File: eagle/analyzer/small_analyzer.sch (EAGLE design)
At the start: 19 parts, among them IC1 MCP604ST, IC2 TPS77301

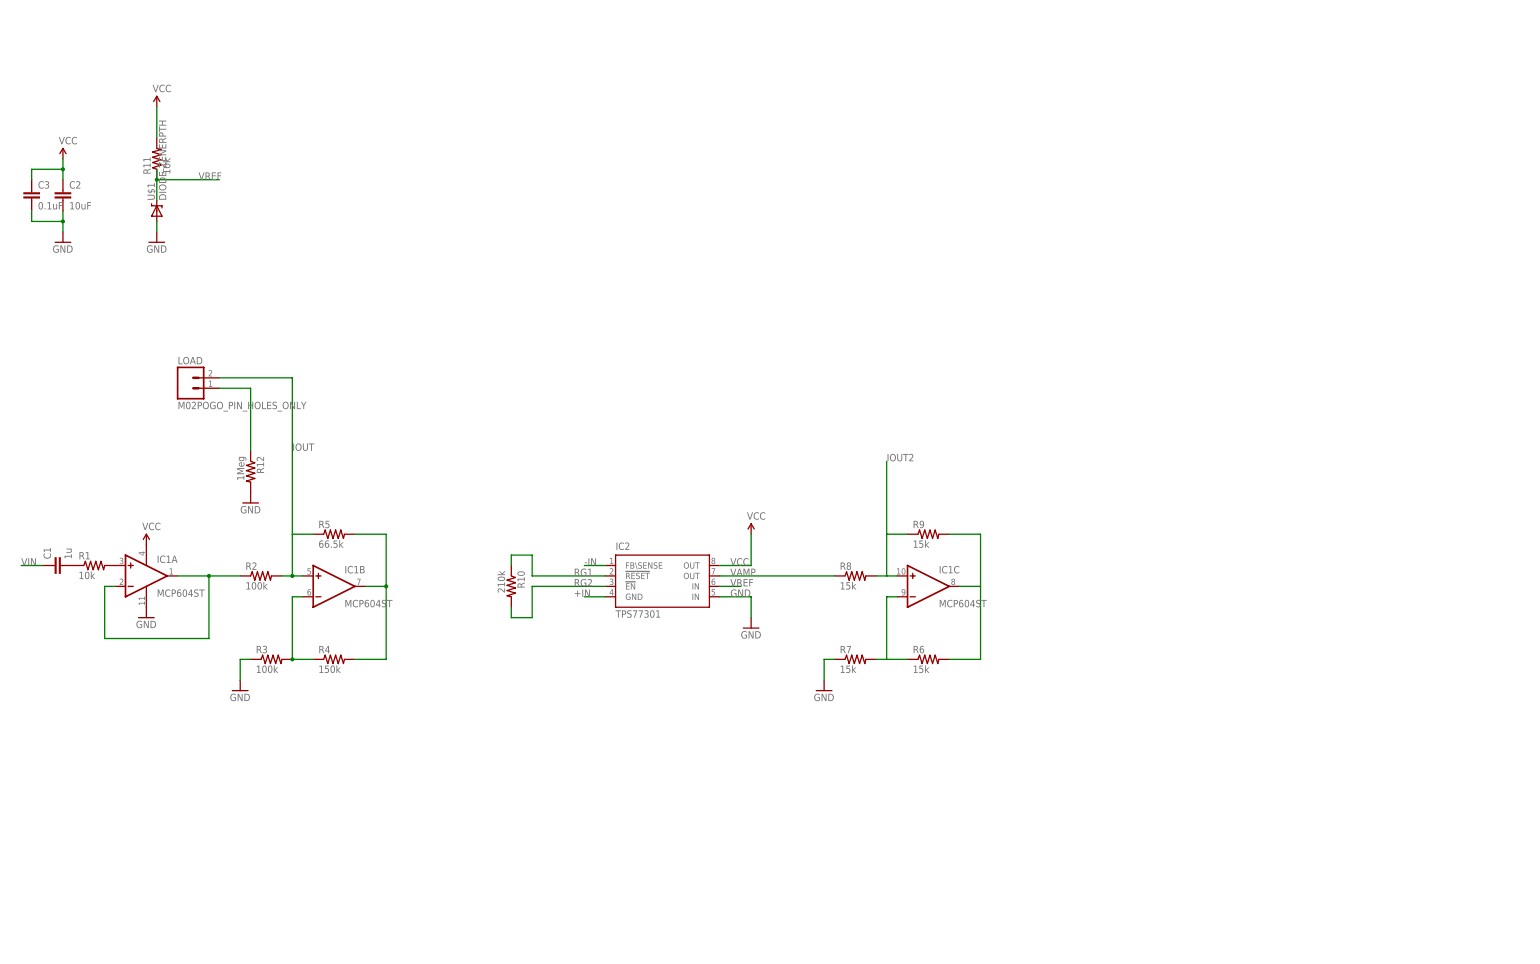
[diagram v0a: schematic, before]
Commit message: added analyzer ic with mcu
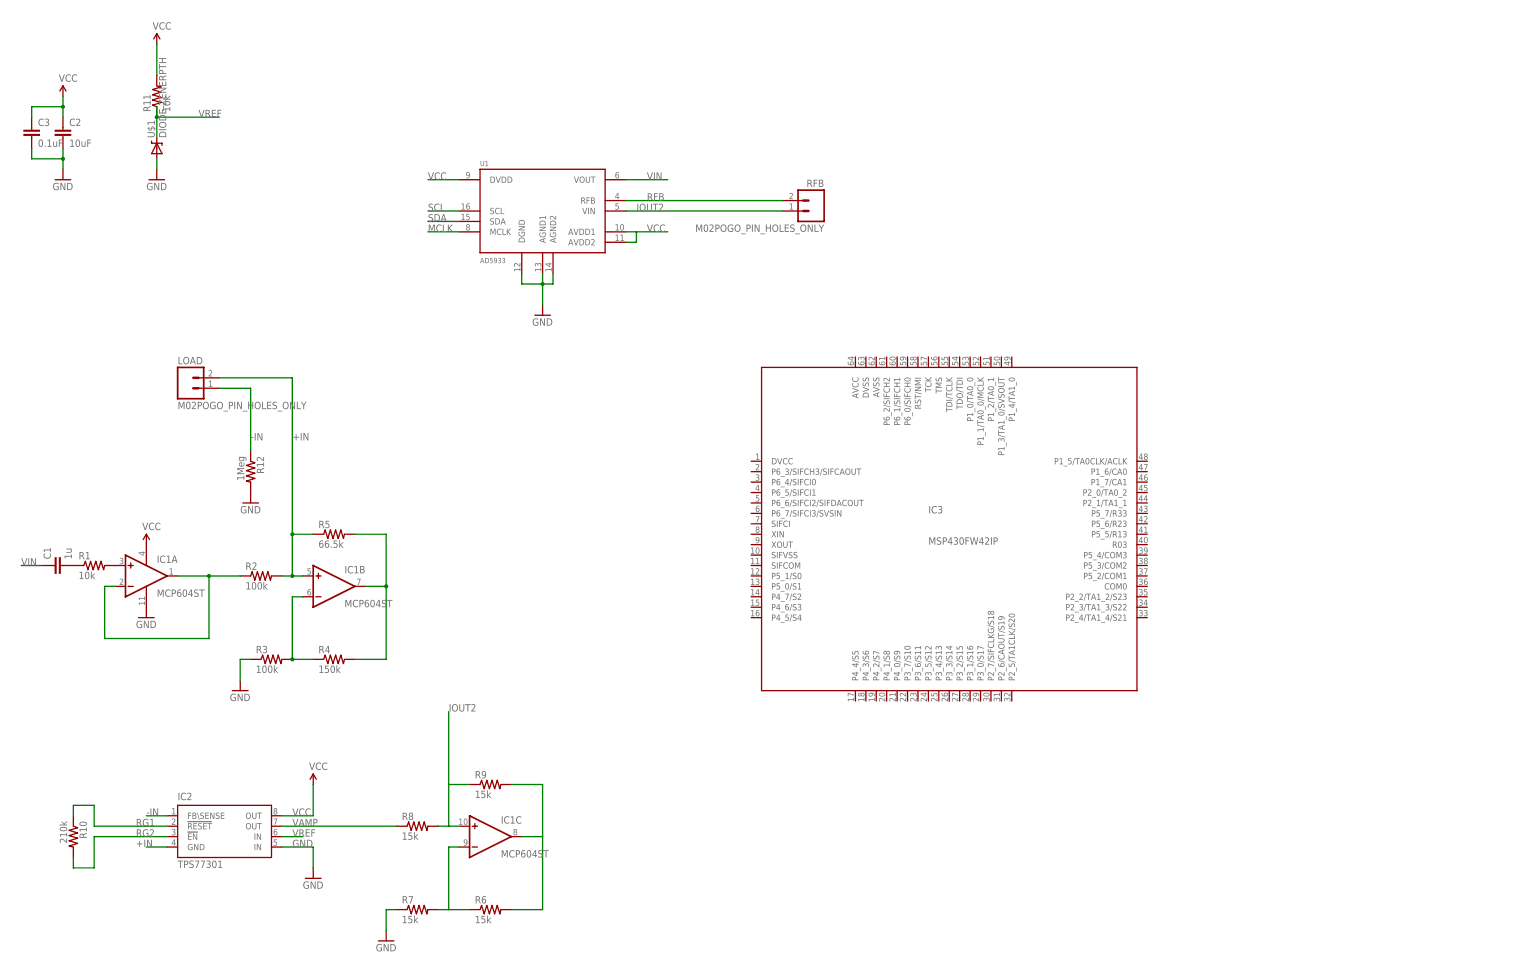
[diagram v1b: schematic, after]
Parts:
- added IC3: MSP430FW42IP, texas:MSP430FW42IP
- added RFB: M02POGO_PIN_HOLES_ONLY, SparkFun-Connectors:M02POGO_PIN_HOLES_ONLY
- added U1: AD5933, kblom:AD5933
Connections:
- removed net IOUT: IC1B.+IN, LOAD.2, R2.2, R5.1
- removed net N$4: LOAD.1, R12.1
- new net MCLK: U1.MCLK
- new net RFB: RFB.2, U1.RFB
- new net SCL: U1.SCL
- new net SDA: U1.SDA
- net +IN: now also IC1B.+IN, LOAD.2, R2.2, R5.1
- net -IN: now also LOAD.1, R12.1
- net GND: now also U1.AGND1, U1.AGND2, U1.DGND
- net IOUT2: now also RFB.1, U1.VIN
- net VCC: now also U1.AVDD1, U1.AVDD2, U1.DVDD
- net VIN: now also U1.VOUT
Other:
- moved on the sheet: C2, C3, IC1C, IC2, R10, R11, R6, R7, R8, R9, U$1

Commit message: added ground planes, expanded board, changed mcu to atmega328
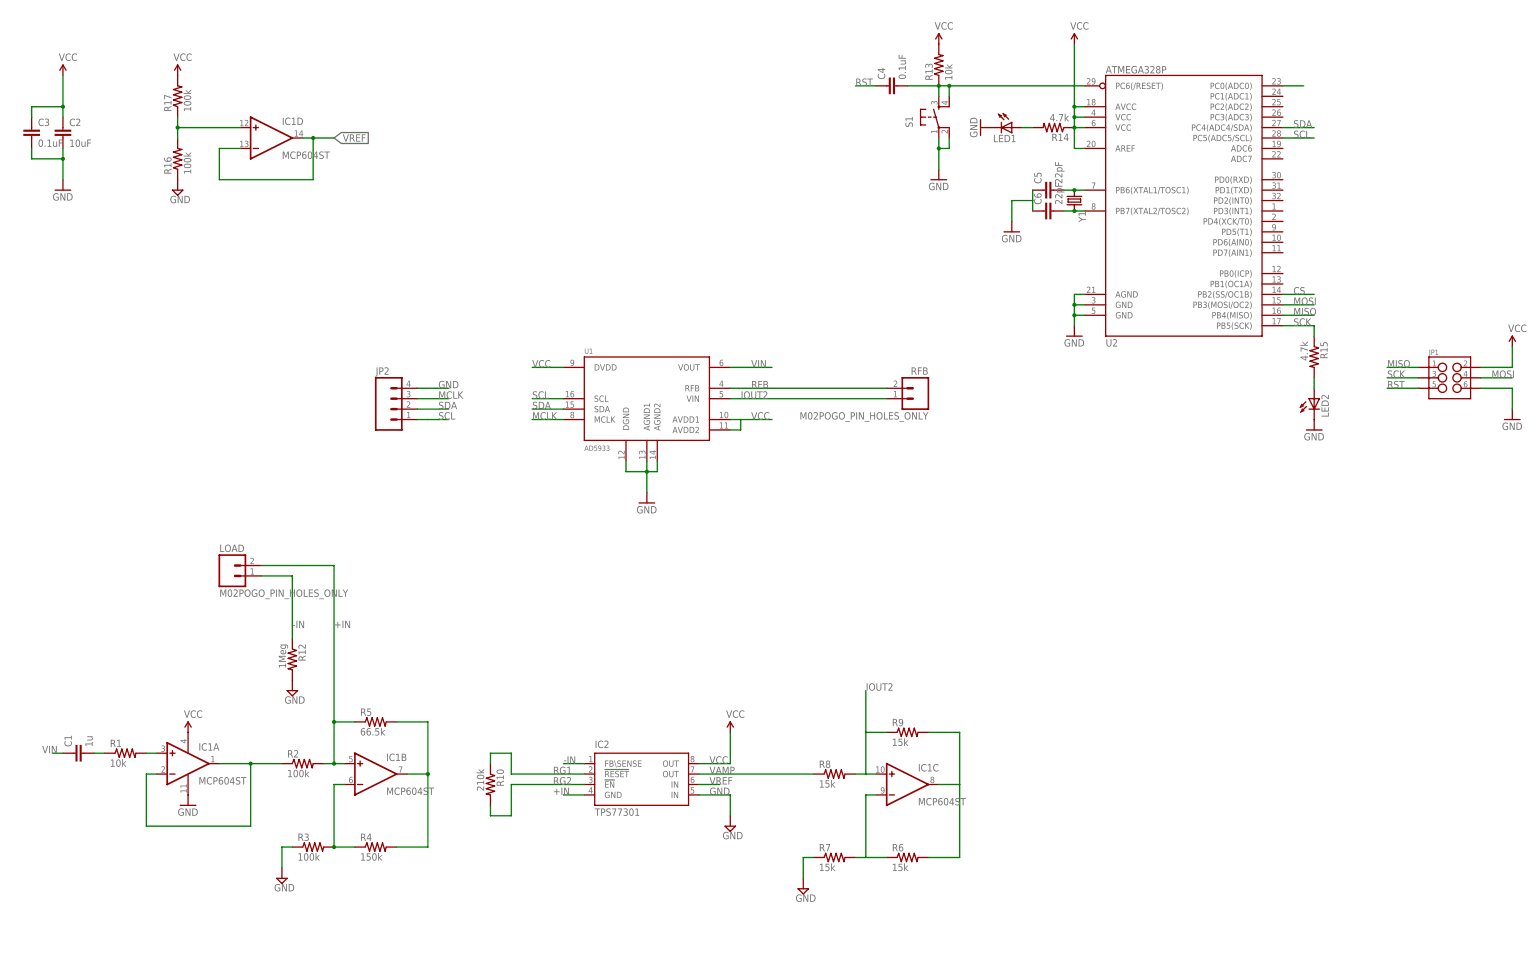
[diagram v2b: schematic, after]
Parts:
- removed IC3: MSP430FW42IP, texas:MSP430FW42IP
- removed R11: 10k, SparkFun-Passives:RESISTOR0603-RES
- removed U$1: DIODE-ZENERPTH, SparkFun-DiscreteSemi:DIODE-ZENERPTH
- added C4: 0.1uF, SparkFun-Passives:CAP0805
- added C5, C6: 22pF, SparkFun-Passives:CAP0805
- added JP1: (no value), SparkFun-Connectors:M03X2NO_SILK
- added JP2: (no value), SparkFun-Connectors:M04PTH
- added LED1, LED2: (no value), SparkFun-LED:LED0603
- added R13: 10k, SparkFun-Passives:RESISTOR0805-RES
- added R14, R15: 4.7k, SparkFun-Passives:RESISTOR0805-RES
- added R16, R17: 100k, SparkFun-Passives:RESISTOR0805-RES
- added S1: (no value), SparkFun-Electromechanical:TAC_SWITCHSMD
- added U2: ATMEGA328P, SparkFun-DigitalIC:ATMEGA328_SMT
- added Y1: (no value), SparkFun-FreqCtrl:CRYSTAL5X3
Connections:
- new net CS: U2.PB2(SS/OC1B)
- new net MISO: JP1.1, U2.PB4(MISO)
- new net MOSI: JP1.4, U2.PB3(MOSI/OC2)
- new net N$10: LED2.A, R15.2
- new net N$11: C4.2, R13.1, S1.3, S1.4, U2.PC6(/RESET)
- new net N$12: LED1.A, R14.2
- new net N$15: IC1D.+IN, R16.2, R17.1
- new net N$17: U2.PC0(ADC0)
- new net N$4: C5.2, U2.PB6(XTAL1/TOSC1), Y1.1
- new net N$9: C6.2, U2.PB7(XTAL2/TOSC2), Y1.2
- new net RST: C4.1, JP1.5
- new net SCK: JP1.3, R15.1, U2.PB5(SCK)
- net GND: now also C5.1, C6.1, JP1.6, JP2.4, LED1.C, LED2.C, R16.1, S1.1, S1.2, U2.AGND, U2.GND@1, U2.GND@2; no longer U$1.A
- net MCLK: now also JP2.3
- net SCL: now also JP2.1, U2.PC5(ADC5/SCL)
- net SDA: now also JP2.2, U2.PC4(ADC4/SDA)
- net VCC: now also JP1.2, R13.2, R14.1, R17.2, U2.AREF, U2.AVCC, U2.VCC@1, U2.VCC@2; no longer R11.2
- net VREF: now also IC1D.-IN, IC1D.OUT; no longer R11.1, U$1.C
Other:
- moved on the sheet: C1, IC1A, IC1B, IC1C, IC2, LOAD, R1, R10, R12, R2, R3, R4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

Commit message: updated
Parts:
- removed C3: 0.1uF, SparkFun-Passives:CAP0603-CAP
- removed LOAD, RFB: M02POGO_PIN_HOLES_ONLY, SparkFun-Connectors:M02POGO_PIN_HOLES_ONLY
- added C7: 10uF, SparkFun-Passives:CAP0603-CAP
- added C8: 0.1uF, SparkFun-Passives:CAP0603-CAP
- added IC3: TPS77350, texas:TPS77350
- added JP3: (no value), SparkFun-Connectors:M04PTH
- added JP4: (no value), SparkFun-Connectors:ARDUINO_SERIAL_PROGRAMLOCK
- C2: value 10uF -> 0.1uF
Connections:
- new net RXI: JP4.TXO, U2.PD0(RXD)
- new net TXO: JP4.RXI, U2.PD1(TXD)
- new net VBAT: C7.1, C8.1, IC3.!RESET, JP4.VCC
- net +IN: now also JP3.3; no longer LOAD.2
- net -IN: now also JP3.4; no longer LOAD.1
- net GND: now also C7.2, C8.2, IC3.GND, JP4.CTS, JP4.GND; no longer C3.2
- net IOUT2: now also JP3.1; no longer RFB.1
- net RFB: now also JP3.2; no longer RFB.2
- net RST: now also JP4.DTR
- net VCC: now also IC3.OUT@1; no longer C3.1
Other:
- note added: "AD8236_8MSOP"
- note added: "ADR423_8MSOP"
- moved on the sheet: C2, R12

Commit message: fixed drc laws
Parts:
- added S2: (no value), SparkFun-Electromechanical:TAC_SWITCHSMD
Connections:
- new net N$16: S2.1, S2.2, U2.PC2(ADC2)
- net VCC: now also S2.3, S2.4
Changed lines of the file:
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@@
 <?xml version="1.0" encoding="utf-8"?>
 <!DOCTYPE eagle SYSTEM "eagle.dtd">
-<eagle version="6.5.0">
+<eagle version="6.4">
 <drawing>
 <settings>
@@
 <part name="JP3" library="SparkFun-Connectors" deviceset="M04" device="PTH"/>
 <part name="JP4" library="SparkFun-Connectors" deviceset="ARDUINO_SERIAL_PROGRAM" device="LOCK"/>
+<part name="S2" library="SparkFun-Electromechanical" deviceset="TAC_SWITCH" device="SMD"/>
+<part name="SUPPLY17" library="SparkFun-Aesthetics" deviceset="VCC" device=""/>
 </parts>
 <sheets>
@@
 <instance part="JP3" gate="G$1" x="132.08" y="114.3"/>
 <instance part="JP4" gate="G$1" x="99.06" y="137.16"/>
+<instance part="S2" gate="S" x="342.9" y="236.22" rot="R90"/>
+<instance part="SUPPLY17" gate="G$1" x="342.9" y="248.92"/>
 </instances>
 <busses>
@@
 <junction x="177.8" y="238.76"/>
 </segment>
+<segment>
+<pinref part="S2" gate="S" pin="3"/>
+<wire x1="342.9" y1="241.3" x2="342.9" y2="243.84" width="0.1524" layer="91"/>
+<pinref part="S2" gate="S" pin="4"/>
+<wire x1="342.9" y1="243.84" x2="345.44" y2="243.84" width="0.1524" layer="91"/>
+<wire x1="345.44" y1="243.84" x2="345.44" y2="241.3" width="0.1524" layer="91"/>
+<wire x1="342.9" y1="243.84" x2="342.9" y2="248.92" width="0.1524" layer="91"/>
+<junction x="342.9" y="243.84"/>
+<pinref part="SUPPLY17" gate="G$1" pin="VCC"/>
+</segment>
 </net>
 <net name="GND" class="0">
@@
 </segment>
 </net>
+<net name="N$16" class="0">
+<segment>
+<pinref part="S2" gate="S" pin="1"/>
+<pinref part="S2" gate="S" pin="2"/>
+<wire x1="345.44" y1="231.14" x2="342.9" y2="231.14" width="0.1524" layer="91"/>
+<junction x="342.9" y="231.14"/>
+<pinref part="U2" gate="G$1" pin="PC2(ADC2)"/>
+<wire x1="320.04" y1="231.14" x2="342.9" y2="231.14" width="0.1524" layer="91"/>
+</segment>
+</net>

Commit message: added sweep push button and decoupling caps
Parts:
- added C3: 10uF, SparkFun-Passives:CAP0603-CAP
- added C9: 0.1uF, SparkFun-Passives:CAP0603-CAP
- R4: value 150k -> 100k
- R5: value 66.5k -> 100k
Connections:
- net GND: now also C3.2, C9.2
- net VCC: now also C3.1, C9.1
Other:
- moved on the sheet: U1
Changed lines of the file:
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@@
 <?xml version="1.0" encoding="utf-8"?>
 <!DOCTYPE eagle SYSTEM "eagle.dtd">
-<eagle version="6.4">
+<eagle version="6.5.0">
 <drawing>
 <settings>
@@
 <part name="SUPPLY3" library="SparkFun-Aesthetics" deviceset="VCC" device=""/>
 <part name="GND1" library="SparkFun-Aesthetics" deviceset="GND" device=""/>
-<part name="R4" library="SparkFun-Passives" deviceset="RESISTOR" device="0603-RES" value="150k"/>
-<part name="R5" library="SparkFun-Passives" deviceset="RESISTOR" device="0603-RES" value="66.5k"/>
+<part name="R4" library="SparkFun-Passives" deviceset="RESISTOR" device="0603-RES" value="100k"/>
+<part name="R5" library="SparkFun-Passives" deviceset="RESISTOR" device="0603-RES" value="100k"/>
 <part name="R6" library="SparkFun-Passives" deviceset="RESISTOR" device="0603-RES" value="15k"/>
 <part name="R7" library="SparkFun-Passives" deviceset="RESISTOR" device="0603-RES" value="15k"/>
@@
 <part name="S2" library="SparkFun-Electromechanical" deviceset="TAC_SWITCH" device="SMD"/>
 <part name="SUPPLY17" library="SparkFun-Aesthetics" deviceset="VCC" device=""/>
+<part name="C3" library="SparkFun-Passives" deviceset="CAP" device="0603-CAP" value="10uF"/>
+<part name="C9" library="SparkFun-Passives" deviceset="CAP" device="0603-CAP" value="0.1uF"/>
+<part name="GND2" library="SparkFun-Aesthetics" deviceset="GND" device=""/>
 </parts>
 <sheets>
@@
 <instance part="R10" gate="G$1" x="127" y="66.04" rot="R270"/>
 <instance part="R12" gate="G$1" x="152.4" y="114.3" rot="R270"/>
-<instance part="U1" gate="A" x="165.1" y="160.02"/>
-<instance part="GND8" gate="1" x="165.1" y="134.62"/>
+<instance part="U1" gate="A" x="187.96" y="160.02"/>
+<instance part="GND8" gate="1" x="187.96" y="134.62"/>
 <instance part="U2" gate="G$1" x="294.64" y="210.82"/>
 <instance part="LED1" gate="G$1" x="254" y="226.06" rot="R270"/>
@@
 <instance part="S2" gate="S" x="342.9" y="236.22" rot="R90"/>
 <instance part="SUPPLY17" gate="G$1" x="342.9" y="248.92"/>
+<instance part="C3" gate="G$1" x="139.7" y="162.56"/>
+<instance part="C9" gate="G$1" x="147.32" y="162.56"/>
+<instance part="GND2" gate="1" x="139.7" y="154.94"/>
 </instances>
 <busses>
@@
 <segment>
 <pinref part="U1" gate="A" pin="AVDD1"/>
-<wire x1="185.42" y1="154.94" x2="187.96" y2="154.94" width="0.2032" layer="91"/>
-<wire x1="187.96" y1="154.94" x2="187.96" y2="152.4" width="0.2032" layer="91"/>
+<wire x1="208.28" y1="154.94" x2="210.82" y2="154.94" width="0.2032" layer="91"/>
+<wire x1="210.82" y1="154.94" x2="210.82" y2="152.4" width="0.2032" layer="91"/>
 <pinref part="U1" gate="A" pin="AVDD2"/>
-<wire x1="187.96" y1="152.4" x2="185.42" y2="152.4" width="0.2032" layer="91"/>
-<wire x1="187.96" y1="154.94" x2="195.58" y2="154.94" width="0.2032" layer="91"/>
-<label x="190.5" y="154.94" size="1.778" layer="95"/>
+<wire x1="210.82" y1="152.4" x2="208.28" y2="152.4" width="0.2032" layer="91"/>
+<wire x1="210.82" y1="154.94" x2="218.44" y2="154.94" width="0.2032" layer="91"/>
+<label x="213.36" y="154.94" size="1.778" layer="95"/>
 </segment>
 <segment>
 <pinref part="U1" gate="A" pin="DVDD"/>
-<wire x1="144.78" y1="167.64" x2="137.16" y2="167.64" width="0.2032" layer="91"/>
-<label x="137.16" y="167.64" size="1.778" layer="95"/>
+<wire x1="167.64" y1="167.64" x2="160.02" y2="167.64" width="0.2032" layer="91"/>
+<label x="160.02" y="167.64" size="1.778" layer="95"/>
+<pinref part="C3" gate="G$1" pin="1"/>
+<wire x1="160.02" y1="167.64" x2="147.32" y2="167.64" width="0.1524" layer="91"/>
+<pinref part="C9" gate="G$1" pin="1"/>
+<junction x="147.32" y="167.64"/>
+<wire x1="147.32" y1="167.64" x2="139.7" y2="167.64" width="0.1524" layer="91"/>
+<junction x="139.7" y="167.64"/>
 </segment>
 <segment>
@@
 <segment>
 <pinref part="U1" gate="A" pin="DGND"/>
-<wire x1="160.02" y1="144.78" x2="160.02" y2="142.24" width="0.2032" layer="91"/>
-<wire x1="160.02" y1="142.24" x2="165.1" y2="142.24" width="0.2032" layer="91"/>
+<wire x1="182.88" y1="144.78" x2="182.88" y2="142.24" width="0.2032" layer="91"/>
+<wire x1="182.88" y1="142.24" x2="187.96" y2="142.24" width="0.2032" layer="91"/>
 <pinref part="U1" gate="A" pin="AGND1"/>
-<wire x1="165.1" y1="142.24" x2="165.1" y2="144.78" width="0.2032" layer="91"/>
+<wire x1="187.96" y1="142.24" x2="187.96" y2="144.78" width="0.2032" layer="91"/>
 <pinref part="U1" gate="A" pin="AGND2"/>
-<wire x1="165.1" y1="142.24" x2="167.64" y2="142.24" width="0.2032" layer="91"/>
-<wire x1="167.64" y1="142.24" x2="167.64" y2="144.78" width="0.2032" layer="91"/>
+<wire x1="187.96" y1="142.24" x2="190.5" y2="142.24" width="0.2032" layer="91"/>
+<wire x1="190.5" y1="142.24" x2="190.5" y2="144.78" width="0.2032" layer="91"/>
 <pinref part="GND8" gate="1" pin="GND"/>
-<wire x1="165.1" y1="142.24" x2="165.1" y2="137.16" width="0.2032" layer="91"/>
-<junction x="165.1" y="142.24"/>
+<wire x1="187.96" y1="142.24" x2="187.96" y2="137.16" width="0.2032" layer="91"/>
+<junction x="187.96" y="142.24"/>
 </segment>
 <segment>
@@
 <label x="104.14" y="142.24" size="1.778" layer="95"/>
 </segment>
+<segment>
+<pinref part="C3" gate="G$1" pin="2"/>
+<wire x1="139.7" y1="157.48" x2="139.7" y2="160.02" width="0.1524" layer="91"/>
+<pinref part="C9" gate="G$1" pin="2"/>
+<wire x1="147.32" y1="160.02" x2="139.7" y2="160.02" width="0.1524" layer="91"/>
+<junction x="139.7" y="160.02"/>
+<pinref part="GND2" gate="1" pin="GND"/>
+</segment>
 </net>
 <net name="VIN" class="0">
@@
 <segment>
 <pinref part="U1" gate="A" pin="VOUT"/>
-<wire x1="185.42" y1="167.64" x2="195.58" y2="167.64" width="0.2032" layer="91"/>
-<label x="190.5" y="167.64" size="1.778" layer="95"/>
+<wire x1="208.28" y1="167.64" x2="218.44" y2="167.64" width="0.2032" layer="91"/>
+<label x="213.36" y="167.64" size="1.778" layer="95"/>
 </segment>
 </net>
@@
 <segment>
 <pinref part="U1" gate="A" pin="VIN"/>
-<label x="187.96" y="160.02" size="1.778" layer="95"/>
-<wire x1="185.42" y1="160.02" x2="195.58" y2="160.02" width="0.2032" layer="91"/>
+<label x="210.82" y="160.02" size="1.778" layer="95"/>
+<wire x1="208.28" y1="160.02" x2="218.44" y2="160.02" width="0.2032" layer="91"/>
 </segment>
 <segment>
@@
 <pinref part="R12" gate="G$1" pin="1"/>
 <wire x1="137.16" y1="119.38" x2="152.4" y2="119.38" width="0.1524" layer="91"/>
+<junction x="152.4" y="119.38"/>
 </segment>
 </net>
@@
 <segment>
 <pinref part="U1" gate="A" pin="RFB"/>
-<label x="190.5" y="162.56" size="1.778" layer="95"/>
-<wire x1="185.42" y1="162.56" x2="195.58" y2="162.56" width="0.2032" layer="91"/>
+<label x="213.36" y="162.56" size="1.778" layer="95"/>
+<wire x1="208.28" y1="162.56" x2="218.44" y2="162.56" width="0.2032" layer="91"/>
 </segment>
 <segment>
@@
 <segment>
 <pinref part="U1" gate="A" pin="SCL"/>
-<wire x1="144.78" y1="160.02" x2="137.16" y2="160.02" width="0.2032" layer="91"/>
-<label x="137.16" y="160.02" size="1.778" layer="95"/>
+<wire x1="167.64" y1="160.02" x2="160.02" y2="160.02" width="0.2032" layer="91"/>
+<label x="160.02" y="160.02" size="1.778" layer="95"/>
 </segment>
 <segment>
@@
 <segment>
 <pinref part="U1" gate="A" pin="SDA"/>
-<wire x1="144.78" y1="157.48" x2="137.16" y2="157.48" width="0.2032" layer="91"/>
-<label x="137.16" y="157.48" size="1.778" layer="95"/>
+<wire x1="167.64" y1="157.48" x2="160.02" y2="157.48" width="0.2032" layer="91"/>
+<label x="160.02" y="157.48" size="1.778" layer="95"/>
 </segment>
 <segment>
@@
 <junction x="119.38" y="238.76"/>
 <label x="111.76" y="238.76" size="1.778" layer="95"/>
+<junction x="127" y="238.76"/>
 </segment>
 <segment>
@@
 <segment>
 <pinref part="U1" gate="A" pin="MCLK"/>
-<wire x1="144.78" y1="154.94" x2="137.16" y2="154.94" width="0.1524" layer="91"/>
-<label x="137.16" y="154.94" size="1.778" layer="95"/>
-</segment>
-<segment>
+<wire x1="167.64" y1="154.94" x2="160.02" y2="154.94" width="0.1524" layer="91"/>
+<label x="160.02" y="154.94" size="1.778" layer="95"/>
+</segment>
+<segment>
